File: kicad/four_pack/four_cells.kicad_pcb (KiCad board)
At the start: 2 copper layers, 80 x 75 mm, 40 parts, among them J1 cell_+, J10 bal_even_right, J11 bal_odd_right, J12 cell_+, J13 cell_+, J14 bal_odd_right, J15 bal_even_right, J16 communication, J17 communication, J18 communication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

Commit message: gerber + logo
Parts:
- added LOGO1: Logo_Open_Hardware_Small, logo:batpacked-24, B.Cu at (41.1, 45.7)
- added LOGO2: Logo_Open_Hardware_Small, logo:batpacked-24, B.Cu at (65.0, 56.4)
- added LOGO3: Logo_Open_Hardware_Small, logo:batpacked-24, B.Cu at (82.8, 65.4)
- added LOGO4: Logo_Open_Hardware_Small, logo:batpacked-24, B.Cu at (24.0, 41.0)
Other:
- board text added: "2021"
- board text added: "Four Pack, bat-packed"
- board text added: "From:"
- board text added: "a"
- board text added: "project"
- board text added: "telec william axel"

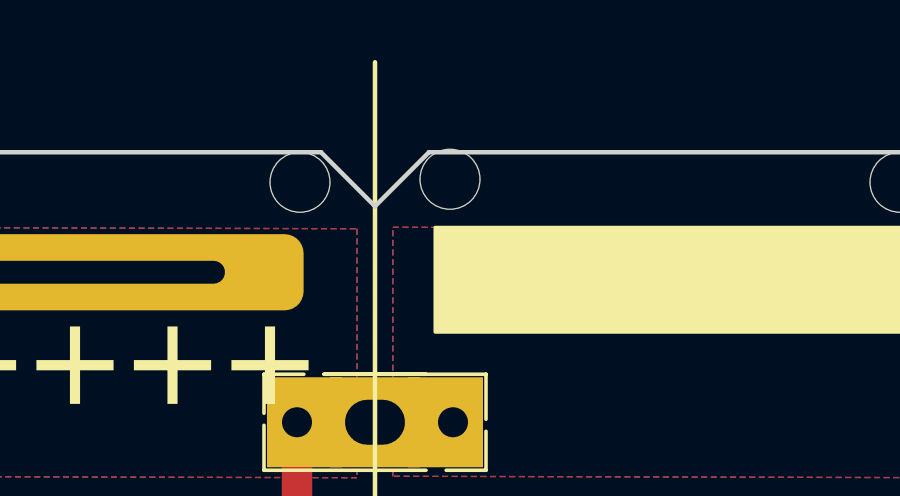
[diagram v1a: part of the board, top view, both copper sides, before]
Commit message: fix silkscreen + hole location
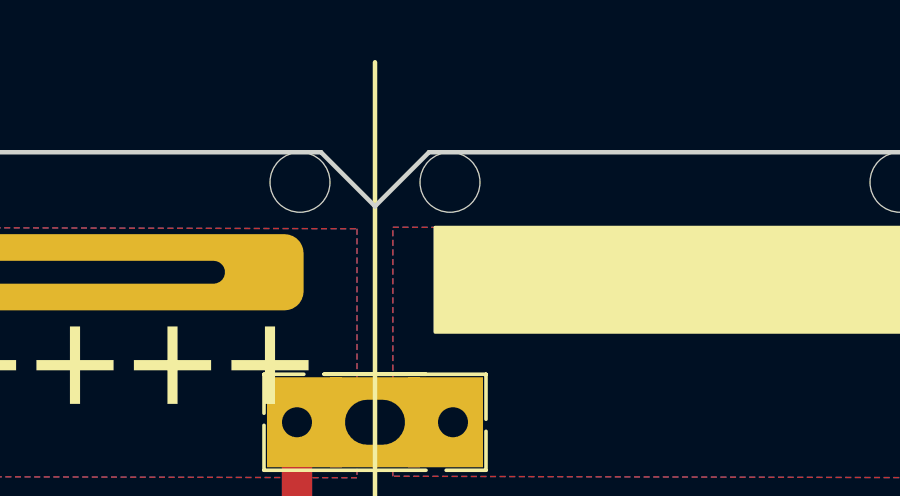
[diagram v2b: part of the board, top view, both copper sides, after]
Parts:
- moved H5 0.10 mm to (34.5, 16.0)
